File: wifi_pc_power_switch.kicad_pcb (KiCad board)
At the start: 2 copper layers, 86.4 x 55.9 mm, 18 parts, among them J1 Conn_01x20_Socket, J2 Conn_01x20_Socket, J3 Conn_01x04_Socket, J4 Conn_01x03_Socket, J5 Conn_01x04_Socket, J6 Conn_01x04_Socket, J7 Conn_01x04_Socket, Q1 BSS123, U1 PicoW, U2 TLP175A

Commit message: Add pull-down to establish default switch state
 - Also force keep-out areas to be where they matter-- for USB and
   antenna, keep-out for both top and bottom layers. For test pads,
   keep-out only on top layer.
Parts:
- added R3: 10k, Resistor_SMD:R_0603_1608Metric_Pad0.98x0.95mm_HandSolder, F.Cu at (184.4, 109.1)
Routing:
- net /EN: track 13.9 -> 18.5 mm
- net GND: track 1.62 -> 3.35 mm, vias 1 -> 2
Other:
- board text added: "WiFi PC Power Switch Gabriel Marcano 2023-11-16 REV: B"
- board text removed: "WiFi PC Power Switch Gabriel Marcano 2023-11-16 REV: A"
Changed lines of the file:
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@@
+  )
+  (footprint "Resistor_SMD:R_0603_1608Metric_Pad0.98x0.95mm_HandSolder" (layer "F.Cu")
+    (at 184.404 109.1165 90)
+    (descr "Resistor SMD 0603 (1608 Metric), square (rectangular) end terminal, IPC_7351 nominal with elongated pad for handsoldering. (Body size source: IPC-SM-782 page 72, https://www.pcb-3d.com/wordpress/wp-content/uploads/ipc-sm-782a_amendment_1_and_2.pdf), generated with kicad-footprint-generator")
+    (tags "resistor handsolder")
+    (property "Digikey Product Number" "")
+    (property "Manufacturer Product Number" "")
+    (property "Mouser Product Number" "")
+    (property "Sheetfile" "wifi_pc_power_switch.kicad_sch")
+    (property "Sheetname" "")
+    (property "ki_description" "Resistor, US symbol")
+    (property "ki_keywords" "R res resistor")
+    (attr smd)
+    (fp_text reference "R3" (at 0 -1.43 90) (layer "F.SilkS")
+        (effects (font (size 1 1) (thickness 0.15)))
+    )
+    (fp_text value "10k" (at 0 1.43 90) (layer "F.Fab")
+        (effects (font (size 1 1) (thickness 0.15)))
+    )
+    (fp_text user "${REFERENCE}" (at 0 0 90) (layer "F.Fab")
+        (effects (font (size 0.4 0.4) (thickness 0.06)))
+    )
+    (fp_line (start -0.254724 -0.5225) (end 0.254724 -0.5225)
+      (stroke (width 0.12) (type solid)) (layer "F.SilkS"))
+    (fp_line (start -0.254724 0.5225) (end 0.254724 0.5225)
+      (stroke (width 0.12) (type solid)) (layer "F.SilkS"))
+    (fp_line (start -1.65 -0.73) (end 1.65 -0.73)
+      (stroke (width 0.05) (type solid)) (layer "F.CrtYd"))
+    (fp_line (start -1.65 0.73) (end -1.65 -0.73)
+      (stroke (width 0.05) (type solid)) (layer "F.CrtYd"))
+    (fp_line (start 1.65 -0.73) (end 1.65 0.73)
+      (stroke (width 0.05) (type solid)) (layer "F.CrtYd"))
+    (fp_line (start 1.65 0.73) (end -1.65 0.73)
+      (stroke (width 0.05) (type solid)) (layer "F.CrtYd"))
+    (fp_line (start -0.8 -0.4125) (end 0.8 -0.4125)
+      (stroke (width 0.1) (type solid)) (layer "F.Fab"))
+    (fp_line (start -0.8 0.4125) (end -0.8 -0.4125)
+      (stroke (width 0.1) (type solid)) (layer "F.Fab"))
+    (fp_line (start 0.8 -0.4125) (end 0.8 0.4125)
+      (stroke (width 0.1) (type solid)) (layer "F.Fab"))
+    (fp_line (start 0.8 0.4125) (end -0.8 0.4125)
+      (stroke (width 0.1) (type solid)) (layer "F.Fab"))
+    (pad "1" smd roundrect (at -0.9125 0 90) (size 0.975 0.95) (layers "F.Cu" "F.Paste" "F.Mask") (roundrect_rratio 0.25)
+      (net 2 "GND") (pintype "passive"))
+    (pad "2" smd roundrect (at 0.9125 0 90) (size 0.975 0.95) (layers "F.Cu" "F.Paste" "F.Mask") (roundrect_rratio 0.25)
+      (net 42 "/EN") (pintype "passive"))
+    (model "${KICAD6_3DMODEL_DIR}/Resistor_SMD.3dshapes/R_0603_1608Metric.wrl"
+      (offset (xyz 0 0 0))
+      (scale (xyz 1 1 1))
+      (rotate (xyz 0 0 0))
+    )
   )
   (footprint "Resistor_SMD:R_0603_1608Metric_Pad0.98x0.95mm_HandSolder" (layer "F.Cu")
@@
     (effects (font (size 1 1) (thickness 0.15)) (justify bottom))
   )
-  (gr_text "WiFi PC Power Switch\nGabriel Marcano\n2023-11-16\nREV: A" (at 186.944 129.032) (layer "F.SilkS")
+  (gr_text "WiFi PC Power Switch\nGabriel Marcano\n2023-11-16\nREV: B" (at 186.944 129.032) (layer "F.SilkS")
     (effects (font (size 1.5 1.5) (thickness 0.2)) (justify left bottom))
   )
   (segment (start 184.912 104.648) (end 187.9725 104.648) (width 0.25) (layer "F.Cu") (net 1))
+  (segment (start 184.404 110.029) (end 184.404 111.76) (width 0.25) (layer "F.Cu") (net 2))
   (segment (start 188.0385 108.1255) (end 187.96 108.204) (width 0.25) (layer "F.Cu") (net 2))
   (segment (start 188.0385 106.614) (end 188.0385 108.1255) (width 0.25) (layer "F.Cu") (net 2))
+  (via (at 184.404 111.76) (size 0.8) (drill 0.4) (layers "F.Cu" "B.Cu") (net 2))
   (via (at 187.96 108.204) (size 0.8) (drill 0.4) (layers "F.Cu" "B.Cu") (net 2))
   (segment (start 189.9135 105.664) (end 189.9135 102.3855) (width 0.25) (layer "F.Cu") (net 3))
@@
   (segment (start 141.199 111.76) (end 144.113 111.76) (width 0.25) (layer "F.Cu") (net 41))
   (segment (start 144.113 111.76) (end 144.272 111.919) (width 0.25) (layer "F.Cu") (net 41))
+  (segment (start 181.864 105.664) (end 184.404 108.204) (width 0.25) (layer "F.Cu") (net 42))
+  (segment (start 180.848 105.664) (end 181.864 105.664) (width 0.25) (layer "F.Cu") (net 42))
   (segment (start 180.848 105.664) (end 182.071 105.664) (width 0.25) (layer "F.Cu") (net 42))
   (segment (start 182.071 105.664) (end 184.912 102.823) (width 0.25) (layer "F.Cu") (net 42))
   (segment (start 172.212 105.664) (end 180.848 105.664) (width 0.25) (layer "F.Cu") (net 42))
-  (zone (net 0) (net_name "") (layer "B.Cu") (hatch edge 0.5)
+  (zone (net 0) (net_name "") (layer "F.Cu") (hatch edge 0.5)
+    (connect_pads (clearance 0))
+    (min_thickness 0.25) (filled_areas_thickness no)
+    (keepout (tracks not_allowed) (vias not_allowed) (pads not_allowed) (copperpour not_allowed) (footprints not_allowed))
+    (fill (thermal_gap 0.5) (thermal_bridge_width 0.5))
+    (polygon
+      (pts
+        (xy 159.512 84.328)
+        (xy 159.512 92.456)
+        (xy 162.052 92.456)
+        (xy 162.052 84.328)
+      )
+    )
+  )
+  (zone (net 0) (net_name "") (layers "F&B.Cu") (hatch edge 0.5)
     (connect_pads (clearance 0))
     (min_thickness 0.25) (filled_areas_thickness no)
@@
     )
   )
-  (zone (net 0) (net_name "") (layer "B.Cu") (hatch edge 0.5)
+  (zone (net 0) (net_name "") (layers "F&B.Cu") (hatch edge 0.5)
     (connect_pads (clearance 0))
     (min_thickness 0.25) (filled_areas_thickness no)
@@
       )
     )
-  )
-  (zone (net 0) (net_name "") (layer "B.Cu") (hatch edge 0.5)
-    (connect_pads (clearance 0))
-    (min_thickness 0.25) (filled_areas_thickness no)
-    (keepout (tracks not_allowed) (vias not_allowed) (pads not_allowed) (copperpour not_allowed) (footprints not_allowed))
-    (fill (thermal_gap 0.5) (thermal_bridge_width 0.5))
-    (polygon
-      (pts
-        (xy 159.512 84.328)
-        (xy 159.512 92.456)
-        (xy 162.052 92.456)
-        (xy 162.052 84.328)
-      )
-    )

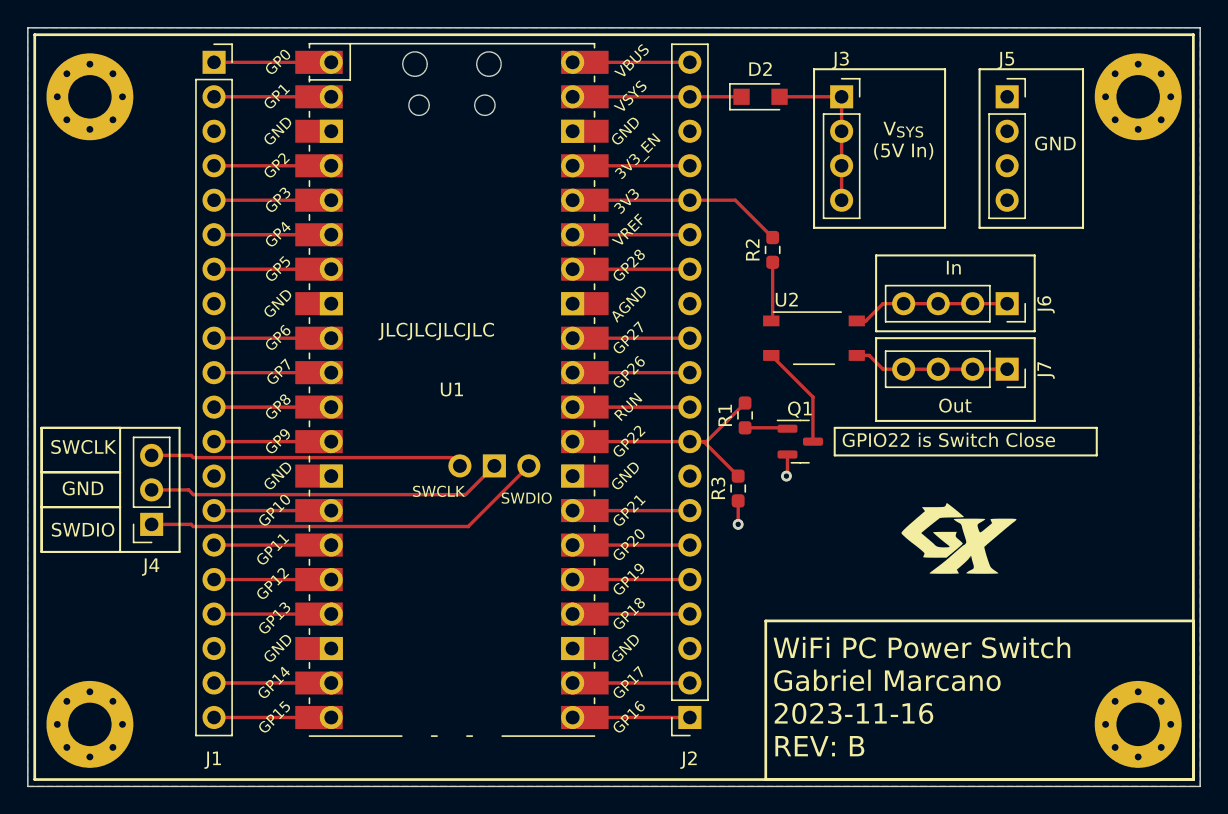
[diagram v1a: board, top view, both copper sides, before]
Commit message: Revision B*: Tentative making everything denser
 - Added 5V notification LED, so it's easier to tell when the board is
   actually powered
 - Condensed the board appreciably
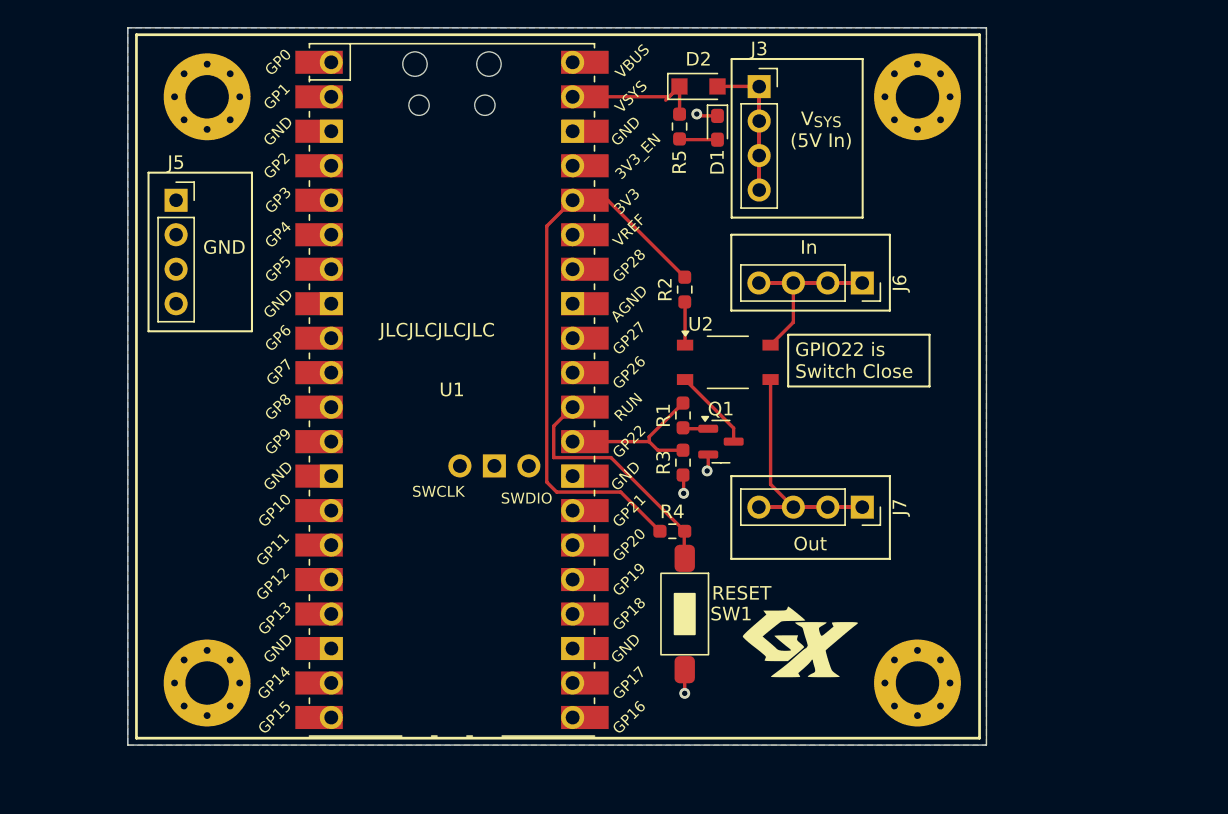
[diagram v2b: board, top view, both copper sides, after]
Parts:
- removed J1, J2: Conn_01x20_Socket, Connector_PinSocket_2.54mm:PinSocket_1x20_P2.54mm_Vertical
- removed J4: Conn_01x03_Socket, Connector_PinSocket_2.54mm:PinSocket_1x03_P2.54mm_Vertical
- added D1: LED, LED_SMD:LED_0603_1608Metric_Pad1.05x0.95mm_HandSolder, F.Cu at (182.9, 82.5)
- added R4: 10k, Resistor_SMD:R_0603_1608Metric_Pad0.98x0.95mm_HandSolder, F.Cu at (179.6, 112.3)
- added R5: 360, Resistor_SMD:R_0603_1608Metric_Pad0.98x0.95mm_HandSolder, F.Cu at (180.1, 82.5)
- added SW1: SW_Push, Marcano:PTS636_SM50_SMTR_LFS, F.Cu at (180.5, 118.4)
- moved J5 61.7 mm to (143.0, 87.9)
- moved H4 16.5 mm to (197.6, 123.4)
- moved H2 16.3 mm to (197.6, 80.3)
- moved J7 14.7 mm to (193.5, 110.5)
- moved G*** 13.9 mm to (189.0, 120.4)
- moved J6 10.8 mm to (193.5, 94.0)
- moved H3 9.16 mm to (145.3, 123.4)
- moved H1 8.64 mm to (145.3, 80.3)
- moved R2 7.11 mm to (180.5, 94.5)
- moved U2 6.59 mm to (183.6, 99.8)
- moved J3 6.12 mm to (186.0, 79.5)
- moved Q1 5.84 mm to (183.1, 105.7)
- moved D2 4.64 mm to (181.5, 79.5)
- moved R1 4.57 mm to (180.3, 103.7)
- moved R3 4.49 mm to (180.3, 107.2)
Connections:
- net Net-(D2-K) renamed /V_{SYS}
- U1 pad 1: Net-(J1-Pin_1) -> unconnected-(U1-GPIO0-Pad1)_1
- U1 pad 10: Net-(J1-Pin_10) -> unconnected-(U1-GPIO7-Pad10)
- U1 pad 11: Net-(J1-Pin_11) -> unconnected-(U1-GPIO8-Pad11)_1
- U1 pad 12: Net-(J1-Pin_12) -> unconnected-(U1-GPIO9-Pad12)_1
- U1 pad 14: Net-(J1-Pin_14) -> unconnected-(U1-GPIO10-Pad14)
- U1 pad 15: Net-(J1-Pin_15) -> unconnected-(U1-GPIO11-Pad15)_1
- U1 pad 16: Net-(J1-Pin_16) -> unconnected-(U1-GPIO12-Pad16)_1
- U1 pad 17: Net-(J1-Pin_17) -> unconnected-(U1-GPIO13-Pad17)_1
- U1 pad 19: Net-(J1-Pin_19) -> unconnected-(U1-GPIO14-Pad19)
- U1 pad 2: Net-(J1-Pin_2) -> unconnected-(U1-GPIO1-Pad2)_1
- U1 pad 20: Net-(J1-Pin_20) -> unconnected-(U1-GPIO15-Pad20)_1
- U1 pad 21: Net-(J2-Pin_1) -> unconnected-(U1-GPIO16-Pad21)_1
- U1 pad 22: Net-(J2-Pin_2) -> unconnected-(U1-GPIO17-Pad22)
- U1 pad 24: Net-(J2-Pin_4) -> unconnected-(U1-GPIO18-Pad24)_1
- U1 pad 25: Net-(J2-Pin_5) -> unconnected-(U1-GPIO19-Pad25)
- U1 pad 26: Net-(J2-Pin_6) -> unconnected-(U1-GPIO20-Pad26)_1
- U1 pad 27: Net-(J2-Pin_7) -> unconnected-(U1-GPIO21-Pad27)_1
- U1 pad 30: Net-(J2-Pin_10) -> /RUN
- U1 pad 31: Net-(J2-Pin_11) -> unconnected-(U1-GPIO26_ADC0-Pad31)_1
- U1 pad 32: Net-(J2-Pin_12) -> unconnected-(U1-GPIO27_ADC1-Pad32)_1
- U1 pad 34: Net-(J2-Pin_14) -> unconnected-(U1-GPIO28_ADC2-Pad34)
- U1 pad 35: Net-(J2-Pin_15) -> unconnected-(U1-ADC_VREF-Pad35)_1
- U1 pad 37: Net-(J2-Pin_17) -> unconnected-(U1-3V3_EN-Pad37)
- U1 pad 4: Net-(J1-Pin_4) -> unconnected-(U1-GPIO2-Pad4)
- U1 pad 40: Net-(J2-Pin_20) -> unconnected-(U1-VBUS-Pad40)
- U1 pad 41: Net-(J4-Pin_3) -> unconnected-(U1-SWCLK-Pad41)
- U1 pad 42: Net-(J4-Pin_2) -> unconnected-(U1-GND-Pad42)
- U1 pad 43: Net-(J4-Pin_1) -> unconnected-(U1-SWDIO-Pad43)
- U1 pad 5: Net-(J1-Pin_5) -> unconnected-(U1-GPIO3-Pad5)
- U1 pad 6: Net-(J1-Pin_6) -> unconnected-(U1-GPIO4-Pad6)_1
- U1 pad 7: Net-(J1-Pin_7) -> unconnected-(U1-GPIO5-Pad7)_1
- U1 pad 9: Net-(J1-Pin_9) -> unconnected-(U1-GPIO6-Pad9)
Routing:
- net Net-(J4-Pin_1): track 29.7 -> 0.00 mm
- net Net-(J4-Pin_2): track 26.3 -> 0.00 mm
- net /V_{3.3}: track 15.9 -> 42.0 mm
- net Net-(J4-Pin_3): track 23.0 -> 0.00 mm
- net /RUN: track 0.00 -> 18.8 mm
- net Net-(J7-Pin_1): track 11.5 -> 25.3 mm
- net Net-(J6-Pin_1): track 11.6 -> 20.5 mm
- net Net-(J2-Pin_7): track 8.64 -> 0.00 mm
- net Net-(J2-Pin_6): track 8.64 -> 0.00 mm
- net Net-(J2-Pin_5): track 8.64 -> 0.00 mm
- net Net-(J2-Pin_4): track 8.64 -> 0.00 mm
- net Net-(J2-Pin_20): track 8.64 -> 0.00 mm
- net Net-(J2-Pin_2): track 8.64 -> 0.00 mm
- net Net-(J2-Pin_17): track 8.64 -> 0.00 mm
- net Net-(J2-Pin_15): track 8.64 -> 0.00 mm
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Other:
- board size 86.4 x 55.9 mm -> 63.2 x 52.8 mm
- board text added: "${TITLE} ${AUTHOR} ${ISSUE_DATE} REV: ${REVISION}"
- board text added: "RESET"
- board text removed: "SWCLK"
- board text removed: "SWDIO"
- board text removed: "WiFi PC Power Switch Gabriel Marcano 2023-11-16 REV: B"

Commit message: Add preliminary pico interface reboot support
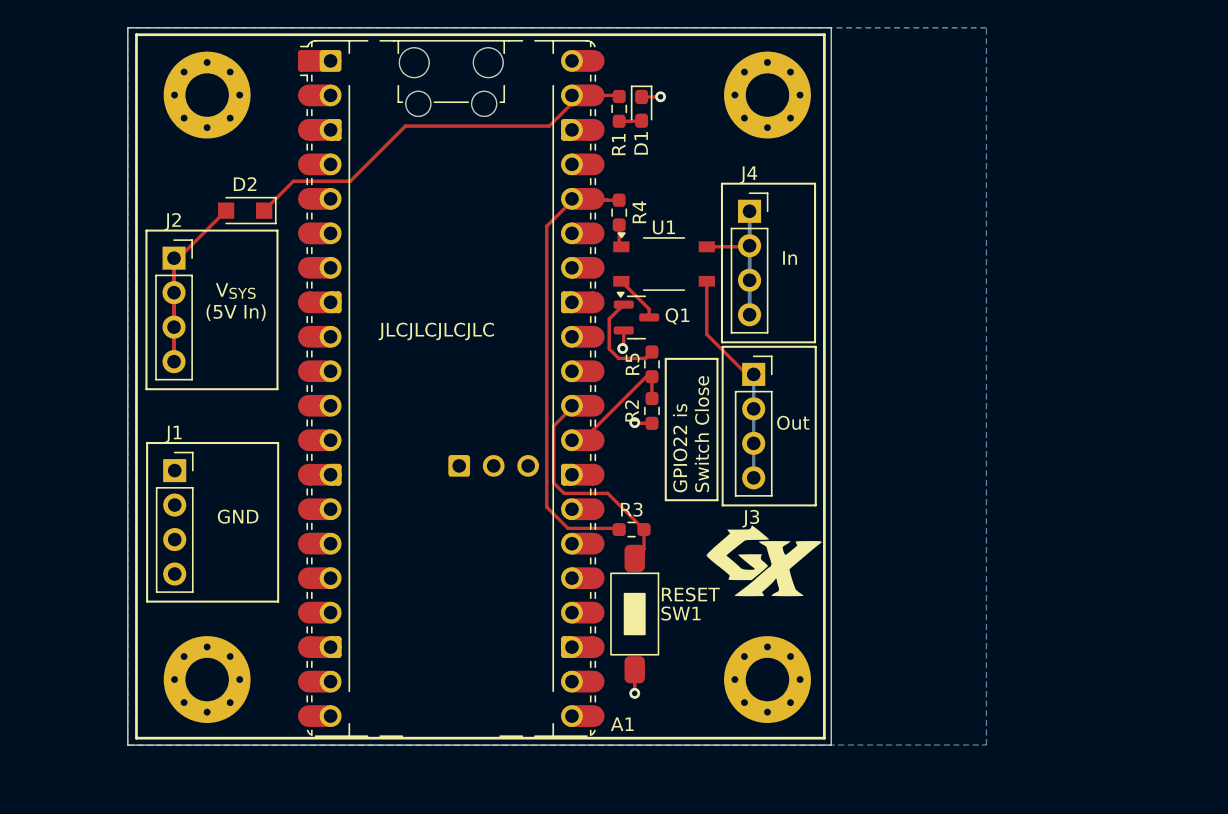
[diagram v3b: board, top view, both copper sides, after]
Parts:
- removed the U1 at (163.3, 101.9)
- added A1: RaspberryPi_Pico_W, Marcano:RaspberryPi_Pico_W_Common_Unspecified, F.Cu at (163.3, 101.8)
- moved J2 44.9 mm to (142.8, 92.2)
- moved D2 34.6 mm to (148.1, 88.6), turned to 180 degrees
- moved J1 19.9 mm to (142.9, 107.8)
- moved J3 12.6 mm to (185.5, 100.7), turned to 0 degrees
- moved Q1 11.1 mm to (176.9, 96.5)
- moved H4 11.1 mm to (186.6, 123.2)
- moved H2 11.0 mm to (186.6, 80.1)
- moved J4 9.84 mm to (185.2, 88.7), turned to 0 degrees
- moved U1 8.63 mm to (178.9, 92.6)
- moved R4 7.44 mm to (175.6, 88.8)
- moved G*** 6.54 mm to (186.3, 114.4)
- moved D1 5.76 mm to (177.3, 81.2)
- moved R1 4.63 mm to (175.6, 81.2)
- moved R2 4.44 mm to (178.1, 103.4)
- moved R5 4.40 mm to (178.1, 100.0), turned to -90 degrees
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- renumbered J5 to J1, J3 to J2, J7 to J3, J6 to J4, R5 to R1, R3 to R2, R4 to R3, R2 to R4, R1 to R5, U2 to U1
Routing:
- net /V_{SYS}: track 11.6 -> 30.5 mm
- net Net-(J3-Pin_1): track 25.3 -> 16.2 mm
- net /V_{3.3}: track 42.0 -> 35.5 mm
- net Net-(Q1-G): track 1.79 -> 7.34 mm
- net /EN: track 12.3 -> 8.63 mm
- net Net-(Q1-D): track 6.05 -> 3.52 mm
- net Net-(D2-A): track 18.3 -> 20.5 mm
- net /RUN: track 18.8 -> 16.6 mm
- net Net-(J4-Pin_1): track 20.5 -> 18.4 mm
- net Net-(R4-Pad1): track 3.15 -> 1.67 mm
- net Net-(D1-A): track 2.49 -> 1.67 mm
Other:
- board size 63.2 x 52.8 mm -> 51.8 x 52.8 mm
